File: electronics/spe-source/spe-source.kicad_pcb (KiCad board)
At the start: 2 copper layers, 38 x 65 mm, 99 parts, among them IC1 AT24C02C-SSHM, J1 CONN_01X05_RA, P2 CONN_01X02, Q1 2N7002P, U1 AP7375-33, U2 MCP65R41T, U3 ATL431LIB, U4 ADIN1110, U5 INA180A3, U6 AP2112K-3.3, U7 TLVM23625RDNR, U8 TPS26625, X1 RH100-25.000-13-F-0715, X2 MICROMOD_FUNCTION_BOARD_EDGE

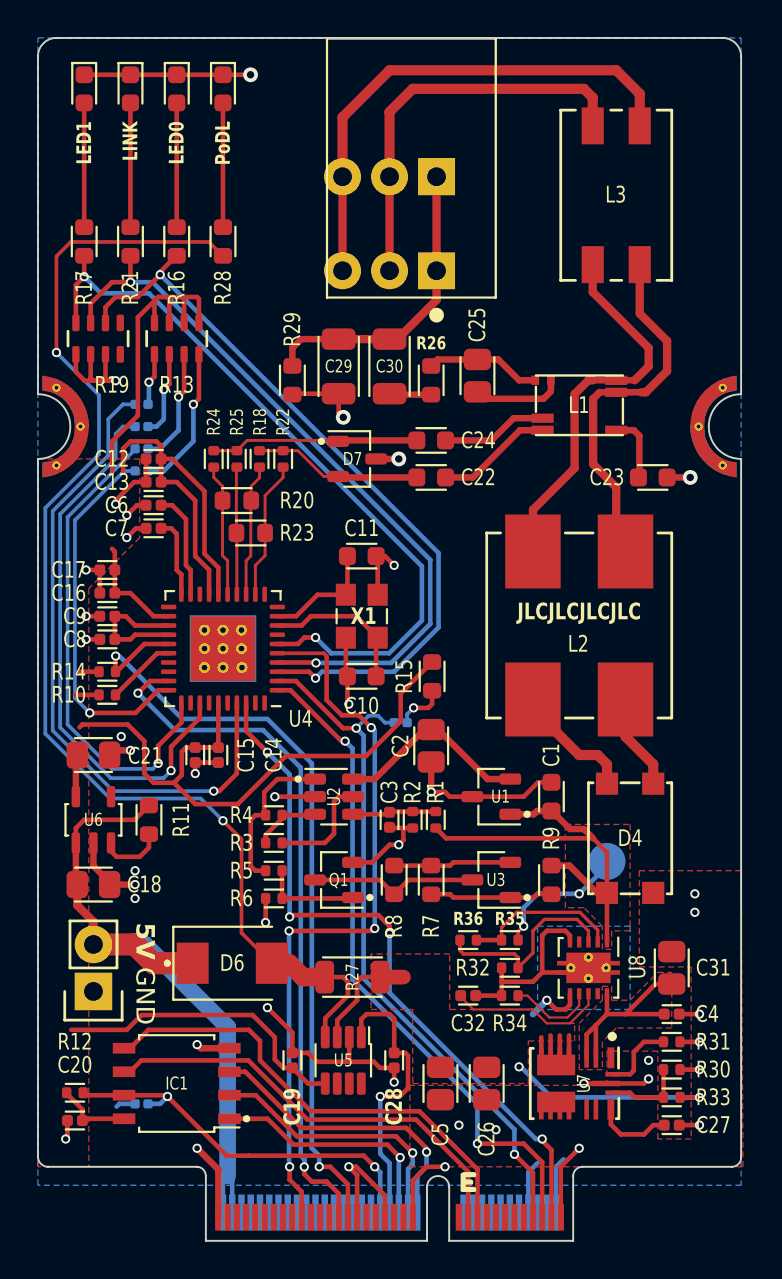
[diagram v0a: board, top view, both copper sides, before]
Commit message: PSE part placement, partial routing
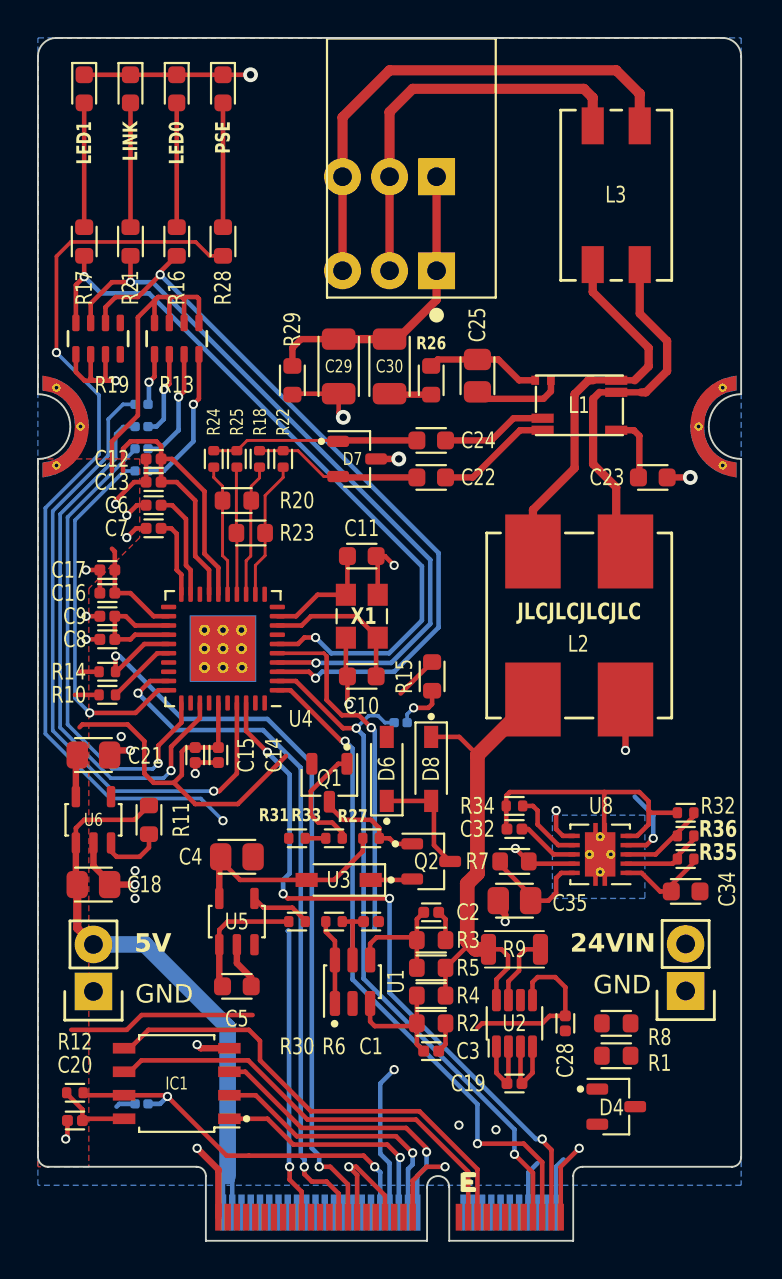
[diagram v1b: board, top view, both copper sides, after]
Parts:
- removed C26: 22u_X5R_2012M, Applidyne_Capacitor:CAPC2012X110N
- removed C27: 1u_X5R_1005M, Applidyne_Capacitor:CAPC1005X60N
- removed C31: 10u_X5R_2012M_50V, Applidyne_Capacitor:CAPC2012X110N
- removed TEST1: PROBE_PAD, Applidyne_Test:TP200
- removed U7: TLVM23625RDNR, Applidyne_QFN:QFN50P450X350X200-11-FCMOD11
- added C34: 1u_X7R_1608M, Applidyne_Capacitor:CAPC1608X90N, F.Cu at (135.0, 85.1)
- added C35: 10u_X5R_2012M_50V, Applidyne_Capacitor:CAPC2012X110N, F.Cu at (125.8, 85.6)
- added D8: 16V_500mW_SOD123, Applidyne_SOD:SOD3715X145N, F.Cu at (121.2, 78.5)
- added P1: CONN_01X02, Applidyne_Connector_Wurth:61300211121, F.Cu at (135.0, 90.5)
- added Q2: DMP6350SQ, Applidyne_SOT:SOT95P240X110-3L16N, F.Cu at (121.2, 83.5)
- C1: value 56n_X7R_1608M -> 100n_X7R_1005M; footprint Applidyne_Capacitor:CAPC1608X90N -> Applidyne_Capacitor:CAPC1005X60N
- C2: value 10u_X7R_2012M -> 1n_X7R_1005M; footprint Applidyne_Capacitor:CAPC2012X110N -> Applidyne_Capacitor:CAPC1005X60N
- C3: value 330p_X7R_1005M -> 1n_X7R_1005M
- C4: value 100n_X7R_1005M -> 10u_X7R_2012M; footprint Applidyne_Capacitor:CAPC1005X60N -> Applidyne_Capacitor:CAPC2012X110N
- C5: value 22u_X5R_2012M -> 1u_X7R_1608M; footprint Applidyne_Capacitor:CAPC2012X110N -> Applidyne_Capacitor:CAPC1608X90N
- D4: value CD-HD2006L -> BAV99; footprint Applidyne_Device:CD-HD2x(L) -> Applidyne_SOT:SOT95P240X110-3L16N
- D6: value B240Q-13-F -> 6V2_500mW_SOD123; footprint Applidyne_SOD:SODFL5436X262N -> Applidyne_SOD:SOD3715X145N
- R1: value 1M_1005M -> 10K0_1608M; footprint Applidyne_Resistor:RESC1005X40N -> Applidyne_Resistor:RESC1608X50N
- R2: value 470K_1005M -> 10K0_1608M; footprint Applidyne_Resistor:RESC1005X40N -> Applidyne_Resistor:RESC1608X50N
- R27: value R01_3216M -> 10K0_1005M; footprint Applidyne_Resistor:RESC3216X60N -> Applidyne_Resistor:RESC1005X40N
- R3: value 10K0_1005M -> 10K0_1608M; footprint Applidyne_Resistor:RESC1005X40N -> Applidyne_Resistor:RESC1608X50N
- R31: value 15K_1005M -> 100K_1005M
- R33: value 40K2_1005M -> 10R_1005M
- R4: value 470K_1005M -> 91K_1608M; footprint Applidyne_Resistor:RESC1005X40N -> Applidyne_Resistor:RESC1608X50N
- R5: value 0R_1005M -> 107K_1608M; footprint Applidyne_Resistor:RESC1005X40N -> Applidyne_Resistor:RESC1608X50N
- R6: value 10K0_1005M -> 47K_1005M
- R7: value 9K09_1608M -> 100K_1608M
- R8: value 20K0_1608M -> 0R_1608M
- R9: value 22R_1608M -> R05_3216M; footprint Applidyne_Resistor:RESC1608X50N -> Applidyne_Resistor:RESC3216X60L
- U1: value AP7375-33 -> TLV6700; footprint Applidyne_SOT:SOT95P240X110-3L16N -> Applidyne_SOT:SOT95P280X145-6L50N
- U2: value MCP65R41T -> INA186A3; footprint Applidyne_SOT:SOT95P240X110-6L16N -> Applidyne_SOT:SOT23-8P65_280X145L45X30N
- U3: value ATL431LIB -> NSI50010YT1G; footprint Applidyne_SOT:SOT95P240X110-3L16N -> Applidyne_SOD:SOD3715X145N
- U5: value INA180A3 -> S-1212-7V; footprint Applidyne_SOT:SOT23-8P65_280X145L45X30N -> Applidyne_SOT:SOT95P280X145-5L30N
- moved C4 25.0 mm to (110.8, 83.2)
- moved R31 23.0 mm to (114.0, 82.2), turned to 180 degrees
- moved R33 23.0 mm to (116.0, 82.2), turned to 0 degrees
- moved R30 21.8 mm to (114.0, 86.8)
- moved R1 16.1 mm to (131.2, 94.0), turned to 180 degrees
- moved U2 15.7 mm to (125.8, 92.2), turned to 0 degrees
- moved D4 14.5 mm to (131.2, 96.8), turned to -90 degrees
- moved R8 14.3 mm to (131.2, 92.2), turned to 0 degrees
- moved D6 13.4 mm to (118.8, 78.5), turned to 90 degrees
- moved R36 13.0 mm to (135.0, 82.1)
- moved R4 12.9 mm to (121.2, 90.8)
- moved C3 12.7 mm to (121.2, 93.8), turned to 0 degrees
- moved R32 12.7 mm to (135.0, 80.9)
- moved U1 12.5 mm to (117.0, 90.0), turned to 0 degrees
- moved C5 12.2 mm to (110.8, 90.2), turned to 0 degrees
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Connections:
- C1 pad 1: /PoDL Device Handling/PoDL+ -> +3.3V
- C2 pad 1: Net-(U1-VOUT) -> Net-(U1-INB-)
- C3 pad 1: Net-(U2--) -> Net-(U1-INA+)
- C4 pad 1: Net-(U7-EN) -> Net-(U5-VOUT)
- C5 pad 1: Net-(U5-S+) -> +24V
- D4 pad 1: /PoDL Device Handling/PoDL+ -> GND
- D4 pad 2: Net-(D4-∿-Pad2) -> +3.3V
- D4 pad 3: Net-(D4-∿-Pad3) -> /MicroMod Function Board/24V_FAULT
- D6 pad A: Net-(U5-S-) -> GND
- D6 pad C: +POWER -> Net-(D6-K)
- L2 pad 1: Net-(D4-∿-Pad3) -> GND
- L2 pad 4: Net-(D4-∿-Pad2) -> /PoDL Supply Handling/PSE+
- R1 pad 1: /PoDL Device Handling/PoDL+ -> /MicroMod Function Board/24V_ENABLE
- R1 pad 2: Net-(U2--) -> GND
- R2 pad 1: Net-(U2--) -> GND
- R2 pad 2: GND -> Net-(U1-INA+)
- R27 pad 1: Net-(U5-S+) -> Net-(U5-VOUT)
- R27 pad 2: Net-(U5-S-) -> Net-(Q1-D)
- R28 pad 1: Net-(U5-S-) -> Net-(D5-PadA)
- R28 pad 2: Net-(D5-PadA) -> /MicroMod Function Board/24V_ENABLE
- R3 pad 1: Net-(U2-REF) -> Net-(U1-INB-)
- R3 pad 2: Net-(U2-+) -> GND
- R30 pad 1: Net-(U7-FB) -> +24V
- R30 pad 2: GND -> Net-(U5-EN)
- R31 pad 1: Net-(U7-RT) -> /MicroMod Function Board/ENABLE_ID_SOURCE
- R33 pad 1: Net-(U5-S+) -> /MicroMod Function Board/ENABLE_ID_SOURCE
- R33 pad 2: Net-(U7-FB) -> Net-(Q1-G)
- R35 pad 1: /PoDL Device Handling/PoDL+ -> +24V
- R4 pad 1: Net-(U2-+) -> /PoDL Supply Handling/PSE+
- R4 pad 2: Net-(R4-Pad2) -> Net-(U1-INA+)
- R5 pad 1: Net-(R4-Pad2) -> /PoDL Supply Handling/PSE+
- R5 pad 2: Net-(Q1-G) -> Net-(U1-INB-)
- R6 pad 1: Net-(Q1-G) -> +3.3V
- R6 pad 2: GND -> /MicroMod Function Board/VID_VALID
- R7 pad 1: Net-(U3-C) -> Net-(U2-S+)
- R7 pad 2: Net-(U3-REF) -> /MicroMod Function Board/24V_FAULT
- R8 pad 1: Net-(U3-REF) -> Net-(X2-F6)
- R8 pad 2: Net-(Q1-D) -> /MicroMod Function Board/24V_FAULT
- R9 pad 1: /PoDL Device Handling/PoDL+ -> Net-(U2-S+)
- R9 pad 2: Net-(U3-C) -> /PoDL Supply Handling/PSE+
- U1 pad 1: /PoDL Device Handling/PoDL+ -> /MicroMod Function Board/VID_VALID
- U1 pad 2: Net-(U1-VOUT) -> GND
- U1 pad 3: GND -> Net-(U1-INA+)
- U2 pad 1: Net-(R4-Pad2) -> +3.3V
- U2 pad 2: GND -> +3.3V
- U2 pad 3: Net-(U2-+) -> GND
- U2 pad 4: Net-(U2--) -> GND
- U2 pad 5: Net-(U2-REF) -> /MicroMod Function Board/ANALOG
- U2 pad 6: Net-(U1-VOUT) -> unconnected-(U2-NC-Pad6)
- U5 pad 1: /MicroMod Function Board/ANALOG -> +24V
- U5 pad 3: Net-(U5-S+) -> unconnected-(U5-NC-Pad3)
- U5 pad 4: Net-(U5-S-) -> Net-(U5-EN)
- U5 pad 5: +3.3V -> Net-(U5-VOUT)
- U8 pad 1: /PoDL Device Handling/PoDL+ -> +24V
- U8 pad 10: Net-(U7-EN) -> Net-(U2-S+)
- U8 pad 4: unconnected-(U8-~{SHDN}-Pad4) -> /MicroMod Function Board/24V_ENABLE
- U8 pad 9: unconnected-(U8-~{FLT}-Pad9) -> /MicroMod Function Board/24V_FAULT
- X2 pad 51: unconnected-(X2-F2/PWM-Pad51) -> /MicroMod Function Board/ENABLE_ID_SOURCE
- X2 pad 53: unconnected-(X2-F3-Pad53) -> /MicroMod Function Board/VID_VALID
- X2 pad 55: unconnected-(X2-F4-Pad55) -> /MicroMod Function Board/24V_ENABLE
- X2 pad 59: unconnected-(X2-F6-Pad59) -> Net-(X2-F6)
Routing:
- net Net-(U5-S-): track 66.0 -> 0.00 mm, vias 2 -> 0
- net /MicroMod Function Board/24V_ENABLE: track 0.00 -> 53.4 mm, vias 0 -> 3
- net /PoDL Device Handling/PoDL+: track 31.0 -> 0.00 mm, vias 2 -> 0
- net /PoDL Supply Handling/PSE+: track 0.00 -> 26.0 mm
- net Net-(U5-S+): track 25.4 -> 0.00 mm, vias 2 -> 0
- net GND: track 115.0 -> 92.0 mm, vias 43 -> 30
- net +24V: track 0.00 -> 12.2 mm
- net Net-(U5-VOUT): track 0.00 -> 11.9 mm
- net Net-(U7-EN): track 11.9 -> 0.00 mm
- net Net-(U1-VOUT): track 10.7 -> 0.00 mm
- net Net-(U2-S+): track 0.00 -> 10.2 mm
- net Net-(R4-Pad2): track 8.63 -> 0.00 mm
- net +3.3V: track 103.7 -> 96.5 mm
- net Net-(U1-INA+): track 0.00 -> 6.82 mm
- net Net-(D4-∿-Pad2): track 6.79 -> 0.00 mm
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- removed copper zone on F.Cu, net /PoDL Device Handling/PoDL+
- removed copper zone on F.Cu, net GND
- removed copper zone on F.Cu, net Net-(U5-S+)
- removed copper zone on F.Cu, net Net-(U7-EN)
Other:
- board text added: "24VIN"
- board text added: "PSE"
- board text added: "SINGLE PAIR ETHERNET PSE MICROMOD FUNCTION BOARD PoDL CLASS 10|11|12"
- board text removed: "PoDL"
- board text removed: "PoDL RAW"
- board text removed: "SINGLE PAIR ETHERNET MICROMOD FUNCTION BOARD PoDL CLASS 10|11|12"

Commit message: PSE routing spaghetti complete
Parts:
- moved R1 48.1 mm to (111.8, 50.0), turned to 90 degrees
- moved R8 13.0 mm to (118.6, 95.2)
- moved D4 1.70 mm to (130.0, 95.6)
- turned R30 to 180 degrees
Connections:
- X2 pad 51: /MicroMod Function Board/ENABLE_ID_SOURCE -> /MicroMod Function Board/VID_VALID
- X2 pad 53: /MicroMod Function Board/VID_VALID -> /MicroMod Function Board/ENABLE_ID_SOURCE
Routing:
- net /MicroMod Function Board/24V_ENABLE: track 53.4 -> 104.4 mm, vias 3 -> 6
- net +3.3V: track 96.5 -> 133.1 mm, vias 0 -> 5
- net /MicroMod Function Board/24V_FAULT: track 3.52 -> 31.8 mm, vias 1 -> 4
- net +24V: track 12.2 -> 37.6 mm, vias 0 -> 2
- net GND: track 92.0 -> 117.3 mm, vias 30 -> 44
- net /MicroMod Function Board/ENABLE_ID_SOURCE: track 1.11 -> 22.0 mm, vias 0 -> 2
- net Net-(X2-F6): track 0.00 -> 13.0 mm, vias 0 -> 2
- net /MicroMod Function Board/VID_VALID: track 4.63 -> 16.3 mm
- net /MicroMod Function Board/ANALOG: track 17.9 -> 25.3 mm
- net /Ethernet MAC+PHY/~{RESET}: track 34.7 -> 37.6 mm, vias 2 -> 4
- net /Ethernet MAC+PHY/CIPO: track 38.2 -> 39.5 mm
- net /Ethernet MAC+PHY/COPI: track 36.4 -> 35.2 mm
- net /Ethernet MAC+PHY/~{CS}: track 38.0 -> 37.2 mm
- net Net-(U5-EN): track 3.29 -> 2.49 mm
- net /MicroMod Function Board/SCL: track 23.8 -> 24.4 mm, vias 0 -> 2
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- added copper zone on F.Cu, net +24V
- added copper zone on F.Cu, net GND
- added copper zone on F.Cu, net Net-(U2-S+)

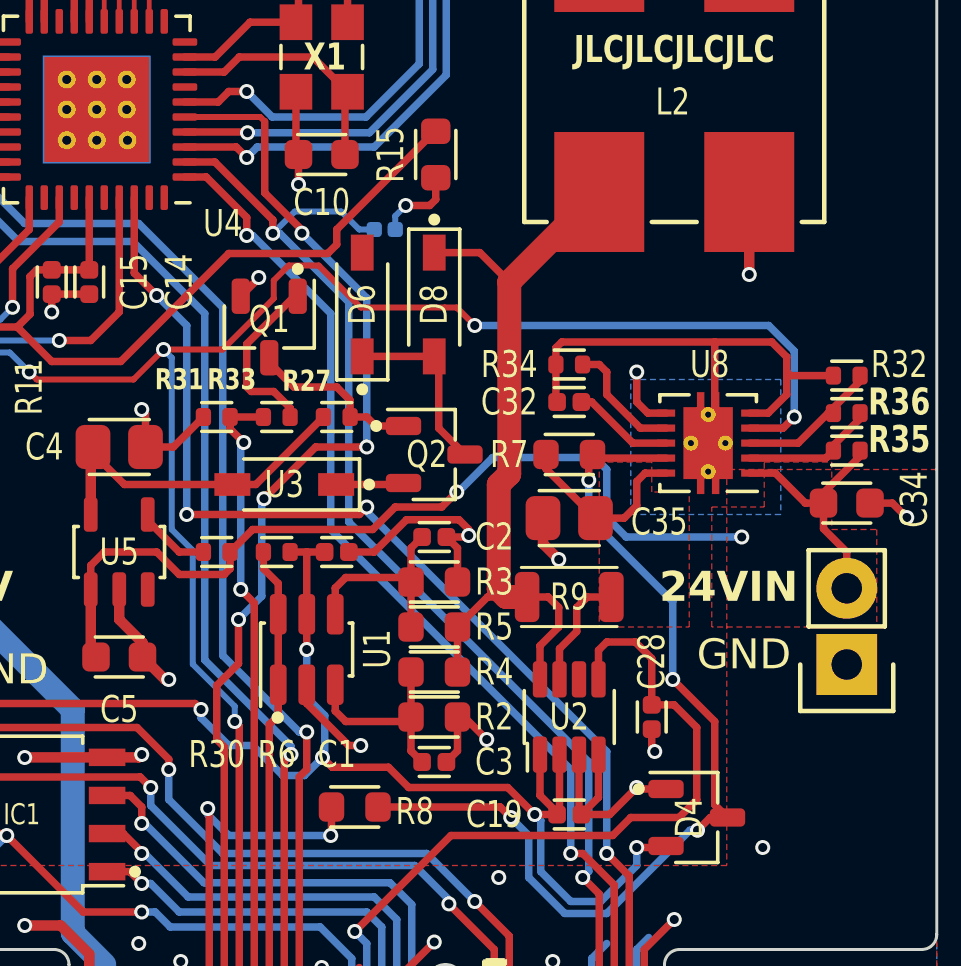
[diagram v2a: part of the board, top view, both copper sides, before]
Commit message: TLV6700 window comparator calculator spreadsheet, PCB export settings
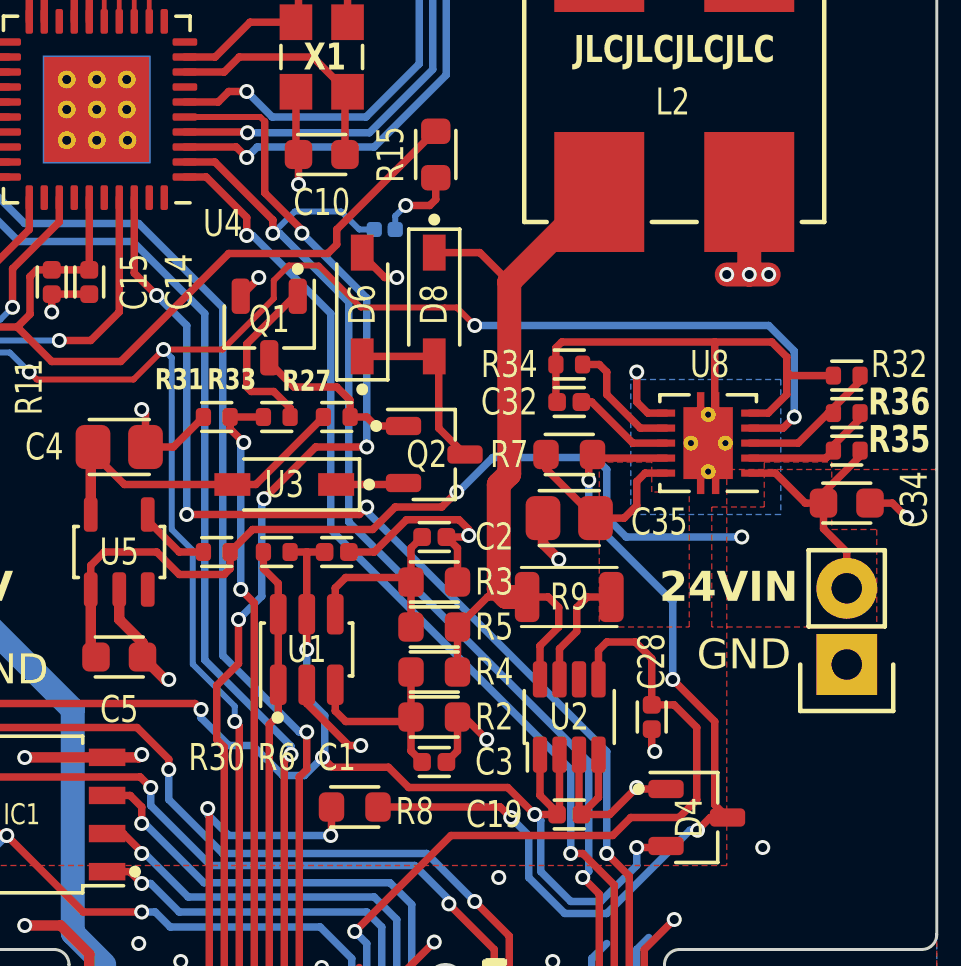
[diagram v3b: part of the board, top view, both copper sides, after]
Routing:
- net GND: track 117.3 -> 120.2 mm, vias 44 -> 47
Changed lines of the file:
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@@
     (pad_to_mask_clearance 0)
     (pcbplotparams
-      (layerselection 0x00010fc_ffffffff)
+      (layerselection 0x00013fc_ffffffff)
       (plot_on_all_layers_selection 0x0000000_00000000)
       (disableapertmacros false)
@@
       (outputformat 1)
       (mirror false)
-      (drillshape 1)
+      (drillshape 0)
       (scaleselection 1)
-      (outputdirectory "")
+      (outputdirectory "output/")
     )
   )
@@
     (property "manf#" "CRCW040210K0FKED")
     (attr smd)
-    (fp_text reference "R30" (at 0 -6.75) (layer "F.SilkS")
+    (fp_text reference "R30" (at 0 -6.85) (layer "F.SilkS")
         (effects (font (size 0.9 0.7) (thickness 0.15)))
     )
@@
     (property "manf#" "RC0402FR-0747KL")
     (attr smd)
-    (fp_text reference "R6" (at 0 -6.75 180) (layer "F.SilkS")
+    (fp_text reference "R6" (at 0 -6.85 180) (layer "F.SilkS")
         (effects (font (size 0.9 0.7) (thickness 0.15)))
     )
@@
     (property "manf#" "TLV6700DDCR")
     (attr smd)
-    (fp_text reference "U1" (at 2.3536 -0.0166 90) (layer "F.SilkS")
+    (fp_text reference "U1" (at 0 0 180) (layer "F.SilkS")
         (effects (font (size 0.9 0.7) (thickness 0.15)))
     )
@@
     (property "manf#" "CGA2B3X7R1H104K050BB")
     (attr smd)
-    (fp_text reference "C1" (at 0 6.75 180) (layer "F.SilkS")
+    (fp_text reference "C1" (at 0 6.85 180) (layer "F.SilkS")
         (effects (font (size 0.9 0.7) (thickness 0.15)))
     )
@@
   (segment (start 103 57.521987) (end 104.2 57.521987) (width 0.25) (layer "F.Cu") (net 1))
   (segment (start 101.595 97.5) (end 101.595 98.405) (width 0.25) (layer "F.Cu") (net 1))
+  (segment (start 118.85 76.77) (end 118.85 76.85) (width 0.25) (layer "F.Cu") (net 1))
   (segment (start 125.4 87) (end 124.875 86.475) (width 0.35) (layer "F.Cu") (net 1))
   (segment (start 103.345 71.5) (end 102.600002 71.5) (width 0.25) (layer "F.Cu") (net 1))
@@
   (segment (start 121.25 99.75) (end 120.25 100.75) (width 0.25) (layer "F.Cu") (net 1))
   (segment (start 102.05 57.05) (end 102.521987 57.521987) (width 0.25) (layer "F.Cu") (net 1))
+  (segment (start 119.6 77.6) (end 120 77.6) (width 0.25) (layer "F.Cu") (net 1))
   (segment (start 116.64 71.41) (end 116.64 73.415) (width 0.25) (layer "F.Cu") (net 1))
   (segment (start 103.875 77.75) (end 104.125 77.5) (width 0.35) (layer "F.Cu") (net 1))
@@
   (segment (start 102.521987 57.521987) (end 104.2 57.521987) (width 0.25) (layer "F.Cu") (net 1))
   (segment (start 103.65 56.1) (end 103.65 57.471987) (width 0.25) (layer "F.Cu") (net 1))
+  (segment (start 131.75 77.5) (end 131 77.5) (width 0.8) (layer "F.Cu") (net 1))
   (segment (start 116.25 58.225) (end 116.25 59.25) (width 0.25) (layer "F.Cu") (net 1))
   (segment (start 128.5 93.3) (end 128.6 93.4) (width 0.25) (layer "F.Cu") (net 1))
   (segment (start 116.25 58.225) (end 113.8 58.225) (width 0.25) (layer "F.Cu") (net 1))
   (segment (start 120.325 85.675) (end 119.25 86.75) (width 0.25) (layer "F.Cu") (net 1))
-  (segment (start 131.75 74.75) (end 131.75 77.5) (width 0.35) (layer "F.Cu") (net 1))
+  (segment (start 131.75 74.75) (end 131.75 77.5) (width 0.8) (layer "F.Cu") (net 1))
+  (segment (start 131.75 77.5) (end 132.4 77.5) (width 0.8) (layer "F.Cu") (net 1))
+  (segment (start 118.85 76.85) (end 119.6 77.6) (width 0.25) (layer "F.Cu") (net 1))
   (segment (start 104.125 77.5) (end 105 77.5) (width 0.35) (layer "F.Cu") (net 1))
   (segment (start 122.4 86) (end 122.075 85.675) (width 0.25) (layer "F.Cu") (net 1))
@@
   (via (at 122.4 86.2) (size 0.5) (drill 0.3) (layers "F.Cu" "B.Cu") (net 1))
   (via (at 102.600002 71.5) (size 0.5) (drill 0.3) (layers "F.Cu" "B.Cu") (net 1))
+  (via (at 132.4 77.5) (size 0.5) (drill 0.3) (layers "F.Cu" "B.Cu") (net 1))
   (via (at 129.25 99) (size 0.5) (drill 0.3) (layers "F.Cu" "B.Cu") (net 1))
   (via (at 118.8 93.2) (size 0.5) (drill 0.3) (layers "F.Cu" "B.Cu") (net 1))
@@
   (via (at 108.5 78.75) (size 0.5) (drill 0.3) (layers "F.Cu" "B.Cu") (net 1))
   (via (at 137 85.6) (size 0.5) (drill 0.3) (layers "F.Cu" "B.Cu") (net 1))
+  (via (at 131 77.5) (size 0.5) (drill 0.3) (layers "F.Cu" "B.Cu") (net 1))
   (via (at 117.5 100.6) (size 0.5) (drill 0.3) (layers "F.Cu" "B.Cu") (net 1))
   (via (at 116.5 59.5) (size 0.8) (drill 0.4) (layers "F.Cu" "B.Cu") (net 1))
@@
   (via (at 111.4 99.8) (size 0.5) (drill 0.3) (layers "F.Cu" "B.Cu") (free) (net 1))
   (via (at 111.5 93.5) (size 0.5) (drill 0.3) (layers "F.Cu" "B.Cu") (net 1))
+  (via (at 120 77.6) (size 0.5) (drill 0.3) (layers "F.Cu" "B.Cu") (net 1))
   (segment (start 128 102.475) (end 128 100) (width 0.25) (layer "B.Cu") (net 1))
   (segment (start 105.25 96.6) (end 104.4 96.6) (width 0.25) (layer "B.Cu") (net 1))
